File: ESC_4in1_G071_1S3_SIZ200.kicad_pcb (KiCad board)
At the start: 4 copper layers, 28 x 28 mm, 182 parts, among them J1 Conn_01x10, U1 STM32G071GBU6, U10 NCP81161MNTBG, U11 SIZ200DT-T1-GE3, U12 NCP81161MNTBG, U13 SIZ200DT-T1-GE3, U14 TPS630701, U15 TPS72733DSE, U16 INA186A2, U17 STM32G071GBU6, U18 NCP81161MNTBG, U19 SIZ200DT-T1-GE3, U2 NCP81161MNTBG, U20 NCP81161MNTBG, U21 STM32G071GBU6, U22 SIZ200DT-T1-GE3, U23 NCP81161MNTBG, U24 SIZ200DT-T1-GE3, U25 NCP81161MNTBG, U26 SIZ200DT-T1-GE3, U27 NCP81161MNTBG, U28 STM32G071GBU6, U29 SIZ200DT-T1-GE3, U3 SIZ200DT-T1-GE3, U30 NCP81161MNTBG, U31 SIZ200DT-T1-GE3, U4 NCP81161MNTBG, U5 SIZ200DT-T1-GE3, U6 NCP81161MNTBG, U7 SIZ200DT-T1-GE3, U8 NCP81161MNTBG, U9 SIZ200DT-T1-GE3

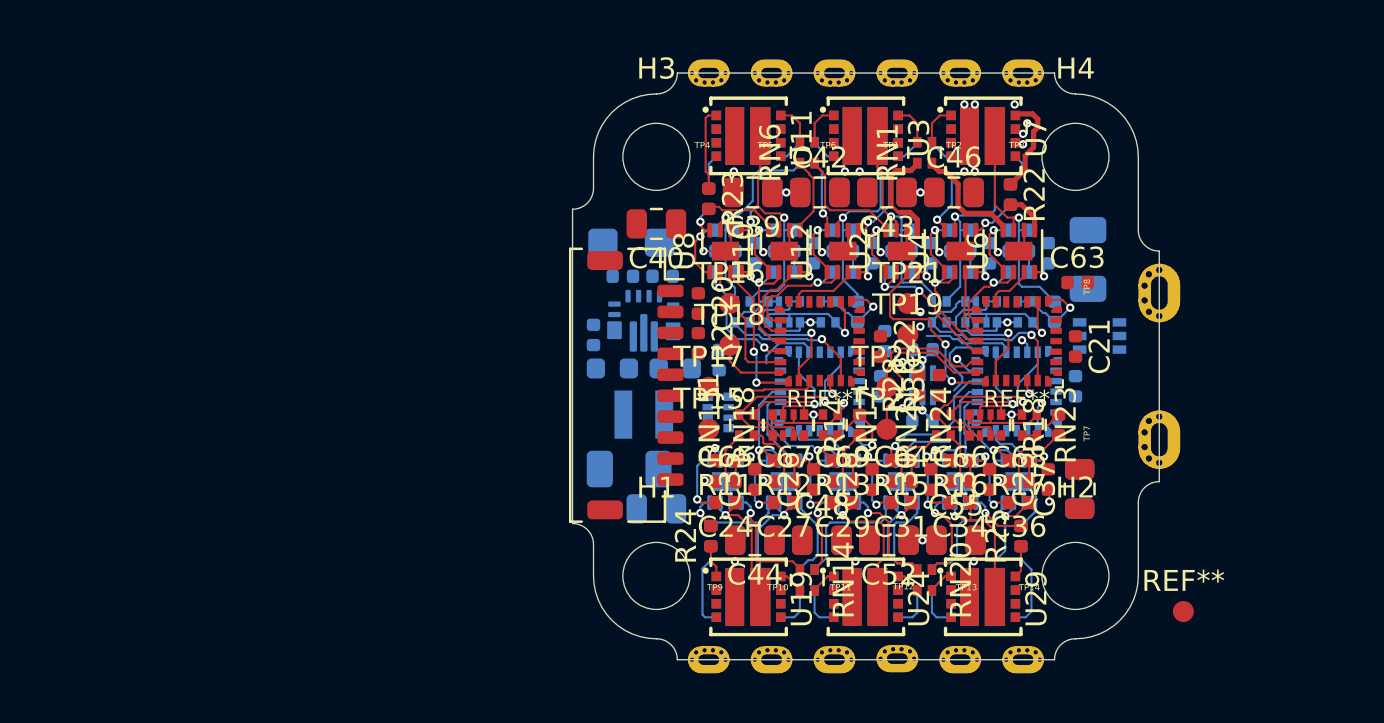
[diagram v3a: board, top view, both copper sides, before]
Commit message: update schematic and layout
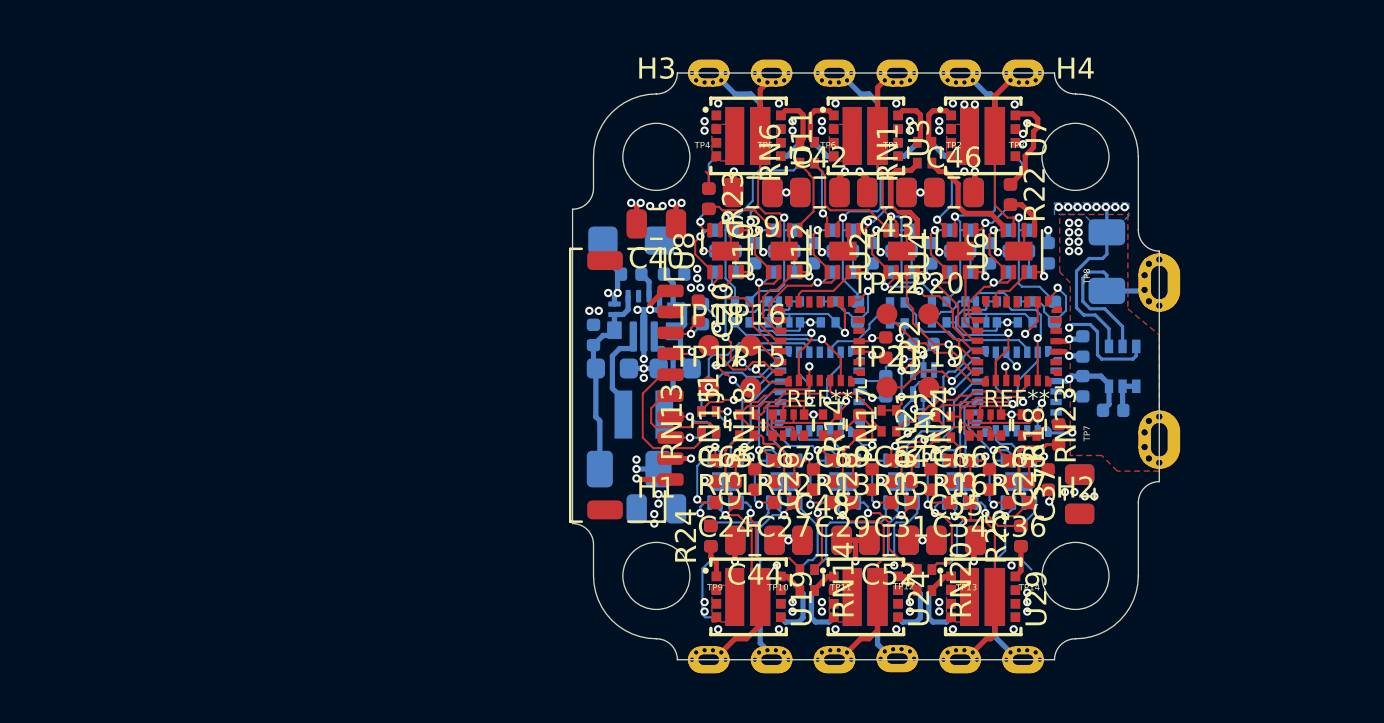
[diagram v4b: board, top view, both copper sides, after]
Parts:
- removed R27, R28, R29, R30: 1k, Resistor_SMD:R_0402_1005Metric
- removed REF**: TestPoint_Pad_D1.0mm_dense, 11_PSoC_FC_whoop:TestPoint_Pad_D1.0mm_dense
- added RN13: 1k, 11_PSoC_FC_whoop:R_Array_Convex_2x0402_dense, F.Cu at (128.5, 77.7)
- added RN16: 1k, 11_PSoC_FC_whoop:R_Array_Convex_2x0402_dense, B.Cu at (128.5, 77.7)
- added RN5: 1k, 11_PSoC_FC_whoop:R_Array_Convex_2x0402_dense, B.Cu at (137.5, 72.5)
- C21, C63, R2: moved to B.Cu
- RN2: footprint 11_PSoC_FC_whoop:R_Array_Convex_4x0402_dense -> 11_PSoC_FC_whoop:R_Array_Convex_2x0402_dense; moved to F.Cu
- moved RN2 8.16 mm to (137.1, 77.6), turned to 270 degrees
- moved C63 6.33 mm to (147.8, 77.1), turned to 180 degrees
- moved TP22 5.50 mm to (137.0, 72.5)
- moved TP21 4.12 mm to (137.0, 76.0)
- moved TP20 4.03 mm to (139.0, 72.5)
- moved TP15 2.83 mm to (130.5, 76.0)
- moved TP19 2.69 mm to (139.0, 76.0)
- moved TP16 2.24 mm to (130.5, 74.0)
- moved U16 1.82 mm to (148.2, 75.0), turned to 90 degrees
- moved R2 1.41 mm to (128.2, 72.5), turned to 90 degrees
- moved TP18 1.00 mm to (128.5, 74.0)
- moved R1 0.91 mm to (147.5, 70.0)
- moved FB2 0.56 mm to (126.8, 70.6), turned to 180 degrees
- moved TP8 0.50 mm to (150.0, 71.0)
- moved R18 0.45 mm to (145.2, 78.2)
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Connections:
- RN2 pad 1: /ESC1_IN -> /ESCx_tele
- RN2 pad 2: /ESC2_IN -> /ESCx_tele
- RN2 pad 3: /ESC3_IN -> /ESC2_tele_o
- RN2 pad 4: /ESC4_IN -> /ESC1_tele_o
- U1 pad 26: Net-(R30-Pad2) -> /ESC1_tele_o
- U17 pad 26: Net-(R28-Pad2) -> /ESC2_tele_o
- U21 pad 26: Net-(R27-Pad2) -> /ESC4_tele_o
- U28 pad 26: Net-(R29-Pad2) -> /ESC3_tele_o
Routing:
- net GND: track 53.2 -> 97.2 mm, vias 26 -> 76
- net Net-(R2-Pad2): track 0.00 -> 25.1 mm, vias 0 -> 2
- net +3V3: track 0.00 -> 21.4 mm, vias 1 -> 4
- net +BATT: track 0.00 -> 18.4 mm, vias 10 -> 44
- net /ESCx_tele: track 0.00 -> 18.0 mm, vias 0 -> 4
- net /ESC1_IN: track 0.00 -> 16.9 mm, vias 0 -> 2
- net /ESC3_IN: track 4.25 -> 17.5 mm, vias 0 -> 2
- net Net-(C13-Pad2): track 0.00 -> 9.12 mm
- net /ESC4_A_EN: track 0.00 -> 9.10 mm, vias 0 -> 2
- net Net-(R1-Pad2): track 0.00 -> 8.35 mm
- net /ESC2_IN: track 3.41 -> 11.1 mm, vias 0 -> 2
- net /ESC1_tele_o: track 0.00 -> 7.42 mm
- net Net-(J1-Pad5): track 0.00 -> 7.35 mm
- net /ESC3_tele_o: track 0.00 -> 7.23 mm
- net Net-(C15-Pad2): track 0.00 -> 5.83 mm
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- added copper zone on F.Cu, net +BATT
- added copper zone on B.Cu, net GND

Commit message: update layout
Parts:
- moved C63 0.15 mm to (147.8, 77.2)
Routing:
- net +BATT: track 18.4 -> 61.3 mm, vias 44 -> 45
- net GND: track 97.2 -> 128.0 mm, vias 76 -> 77
- net /ESC2_IN: track 11.1 -> 5.25 mm, vias 2 -> 0
- net /ESC2_B_GH: track 0.88 -> 5.05 mm
- net /ESC3_C_GL: track 1.32 -> 4.89 mm
- net Net-(C15-Pad2): track 5.83 -> 7.52 mm
- net /ESC4_SWDIO: track 1.76 -> 3.32 mm
- net /ESC4_SWDCLK: track 4.03 -> 5.49 mm
- net +5V: track 40.9 -> 41.7 mm
- net /ESC4_B_GH: track 4.15 -> 4.90 mm, vias 1 -> 0
- net /ESC4_IN: track 8.08 -> 8.78 mm
- net /ESC3_MC: track 3.41 -> 3.97 mm
- added copper zone on F.Cu, net GND

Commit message: update schematic, layout and schematic pdf
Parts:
- L1: value 1u -> 820 nH
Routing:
- added copper zone on In1.Cu_(power), net /ESC3_B
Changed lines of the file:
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@@
       (effects (font (size 1 1) (thickness 0.15)) (justify mirror))
     )
-    (fp_text value 1u (at 0 -2.65) (layer B.Fab)
+    (fp_text value "820 nH" (at 0 -2.65) (layer B.Fab)
       (effects (font (size 1 1) (thickness 0.15)) (justify mirror))
     )
@@
     (polygon
       (pts
-        (xy 150 89) (xy 122 89) (xy 122 61) (xy 150 61)
+        (xy 150 89.5) (xy 122 89.5) (xy 122 61) (xy 150 61)
       )
     )
@@
     (polygon
       (pts
-        (xy 150 89) (xy 122 89) (xy 122 80.5) (xy 144.5 80.5) (xy 145 80)
+        (xy 150 89.5) (xy 122 89.5) (xy 122 80.5) (xy 144.5 80.5) (xy 145 80)
         (xy 145 76.5) (xy 145.5 76) (xy 145.5 74) (xy 145 73.5) (xy 145 70)
         (xy 144.5 69.5) (xy 127 69.5) (xy 123 73.5) (xy 122 73.5) (xy 122 61)
@@
       )
     )
+  )
+  (zone (net 82) (net_name /ESC3_B) (layer "In1.Cu_(power)") (hatch edge 0.508)
+    (connect_pads yes (clearance 0.125))
+    (min_thickness 0.125)
+    (fill yes (arc_segments 32) (thermal_gap 0.508) (thermal_bridge_width 0.508))
+    (polygon
+      (pts
+        (xy 141.75 89.75) (xy 139.25 89.75) (xy 139.25 88.25) (xy 141.75 88.25)
+      )
+    )

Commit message: cosmetic update
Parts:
- added C70: 10u, Capacitor_SMD:C_0402_1005Metric, B.Cu at (133.1, 85.3)
- C13: footprint 11_PSoC_FC_whoop:C_1206_3216Metric_dense -> 11_PSoC_FC_whoop:C_0805_2012Metric_dense
- C37: moved to B.Cu
- moved TP14 22.5 mm to (122.0, 82.5), turned to 270 degrees
- moved TP3 22.5 mm to (150.0, 82.5), turned to 90 degrees
- moved TP4 22.5 mm to (150.0, 67.5), turned to 90 degrees
- moved TP9 22.5 mm to (122.0, 67.5), turned to 270 degrees
- moved TP10 20.8 mm to (122.0, 70.5), turned to 270 degrees
- moved TP2 20.8 mm to (150.0, 79.5), turned to 90 degrees
- moved TP13 20.8 mm to (122.0, 79.5), turned to 270 degrees
- moved TP5 20.8 mm to (150.0, 70.5), turned to 90 degrees
- moved TP8 20.6 mm to (140.0, 89.0), turned to 0 degrees
- moved TP7 20.4 mm to (132.5, 89.0), turned to 0 degrees
- moved H1 20.0 mm to (126.0, 65.0), turned to 270 degrees
- moved H2 20.0 mm to (126.0, 85.0), turned to 270 degrees
- moved H3 20.0 mm to (146.0, 65.0), turned to 270 degrees
- moved H4 20.0 mm to (146.0, 85.0), turned to 270 degrees
- moved TP1 19.9 mm to (150.0, 76.5), turned to 90 degrees
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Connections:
- net Net-(R1-Pad2) renamed /Batt-
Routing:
- net GND: track 128.0 -> 135.6 mm, vias 77 -> 80
- net +BATT: track 61.3 -> 67.6 mm, vias 45 -> 62
- net +3V3: track 21.5 -> 17.8 mm, vias 4 -> 5
- net /ESC2_A: track 14.1 -> 17.7 mm
- net /Batt-: track 8.44 -> 6.89 mm
- net +5V: track 41.7 -> 43.1 mm, vias 18 -> 17
- net /ESCx_tele: track 18.0 -> 19.0 mm
- net /ESC1_B_PWM: track 5.93 -> 4.98 mm
- net Net-(R2-Pad2): track 25.1 -> 25.8 mm
- net /ESC2_A_PWM: track 6.99 -> 6.45 mm
- net /ESC4_IN: track 8.78 -> 9.22 mm, vias 0 -> 2
- added copper zone on B.Cu, net +5V
- added copper zone on B.Cu, net +BATT
- added copper zone on B.Cu, net /Batt-
- added copper zone on F.Cu, net /ESC1_A
- added copper zone on F.Cu, net /ESC1_A_DRVH
- added copper zone on B.Cu, net /ESC1_B
- added copper zone on F.Cu, net /ESC1_C
- added copper zone on B.Cu, net /ESC2_A
- added copper zone on F.Cu, net /ESC2_B
- added copper zone on B.Cu, net /ESC2_C
- added copper zone on B.Cu, net /ESC3_A
- added copper zone on B.Cu, net /ESC3_A_DRVH
- added copper zone on B.Cu, net /ESC3_A_DRVL
- added copper zone on F.Cu, net /ESC3_B
- added copper zone on B.Cu, net /ESC3_C
- added copper zone on F.Cu, net /ESC4_A
- added copper zone on B.Cu, net /ESC4_B
- added copper zone on B.Cu, net /ESC4_B_DRVH
- added copper zone on B.Cu, net /ESC4_B_DRVL
- added copper zone on F.Cu, net /ESC4_C
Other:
- outline, holes or cut-outs redrawn
- rule solder_mask_min_width: 0.05 -> 0.1
- board text added: "+"
- board text added: "-"
- board text added: "ESC-4in1_G071_SIZ200"
- board text added: "Gnd VBat Ibat Tele ESC1 ESC2 ESC3 ESC4 5V Gnd"
- board text added: "crteensy 1-3S 15A"

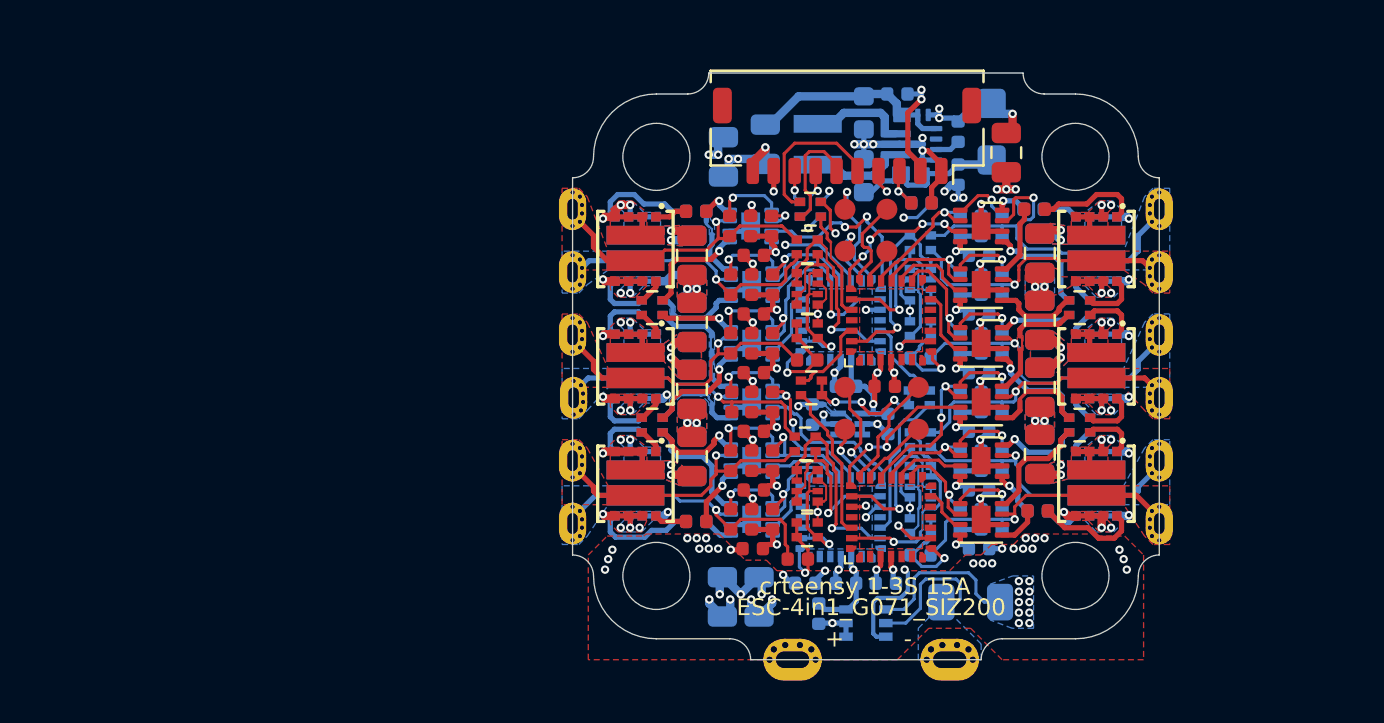
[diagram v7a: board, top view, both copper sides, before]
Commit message: update schematic, layout and doc
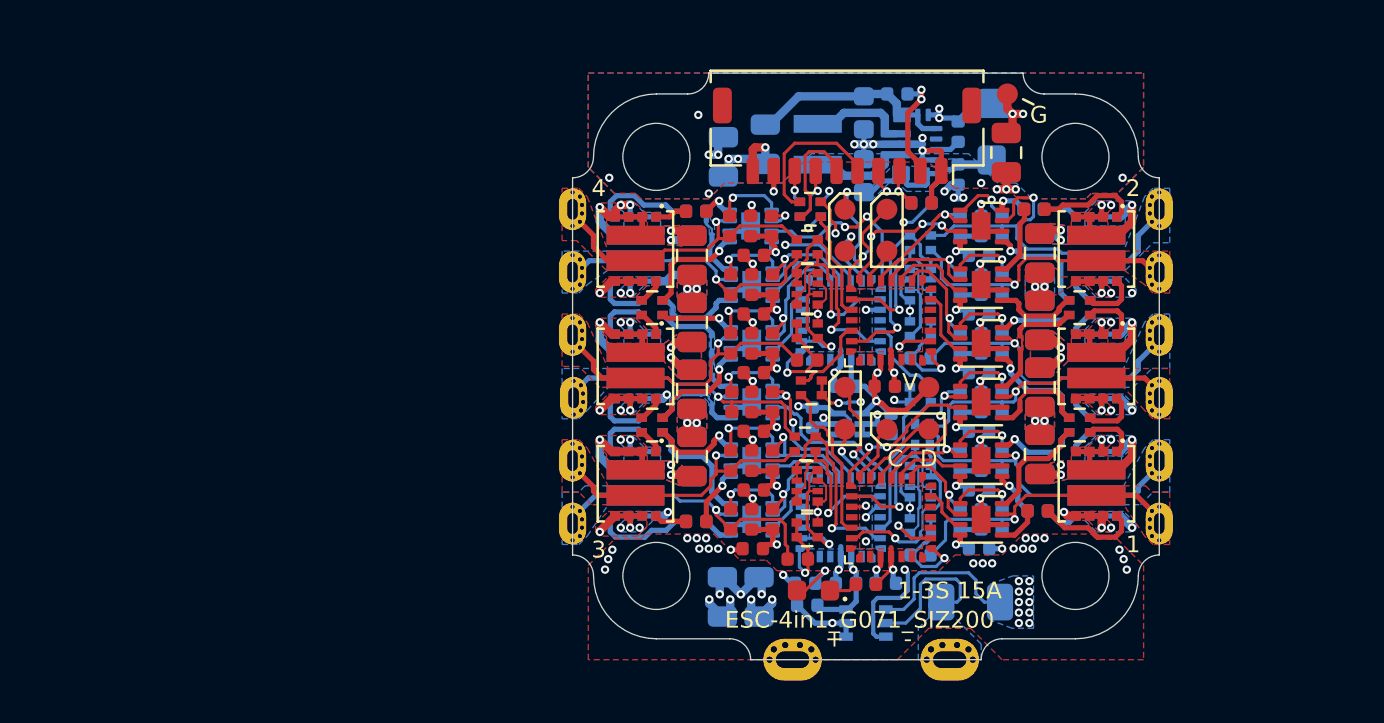
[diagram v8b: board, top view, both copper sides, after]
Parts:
- added D1: LED, LED_SMD:LED_0603_1608Metric, F.Cu at (133.5, 85.7)
- added R27: 1k, Resistor_SMD:R_0402_1005Metric, F.Cu at (136.0, 85.4)
- added TP23: TestPoint, 11_PSoC_FC_whoop:TestPoint_Pad_D1.0mm_dense, F.Cu at (139.0, 76.0)
- added TP24: TestPoint, 11_PSoC_FC_whoop:TestPoint_Pad_D1.0mm_dense, F.Cu at (142.8, 62.0)
- U11, U13, U19, U22, U24, U26, U29, U3, U31, U5, U7, U9: footprint 11_PSoC_FC_whoop:PowerPAIR3.3x3.3 -> 11_PSoC_FC_whoop:PowerPAIR3.3x3.3_splitpaste
- moved TP22 2.50 mm to (137.0, 78.0)
- moved C63 0.68 mm to (133.2, 86.4), turned to 0 degrees
- moved TP20 0.50 mm to (139.0, 78.0)
- moved RN8 0.27 mm to (138.7, 78.2), turned to 270 degrees
- moved RN5 0.16 mm to (138.6, 76.3)
- moved C18 0.15 mm to (133.4, 77.5)
- moved C19 0.15 mm to (137.2, 77.8)
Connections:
- RN8 pad 1: /ESC1_A -> /ESC1_B
- RN8 pad 2: /ESC1_B -> /ESC1_A
- RN8 pad 3: /ESC1_MB -> /ESC1_MA
- RN8 pad 4: /ESC1_MA -> /ESC1_MB
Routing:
- net +BATT: track 67.6 -> 86.1 mm
- net GND: track 135.6 -> 144.0 mm, vias 80 -> 87
- net +3V3: track 17.8 -> 22.0 mm
- net /ESC1_SWDCLK: track 5.41 -> 2.79 mm
- net /ESC1_B: track 14.0 -> 15.7 mm
- net Net-(D1-Pad1): track 0.00 -> 1.35 mm
- net /ESCx_tele: track 19.0 -> 17.8 mm
- net /ESC1_MA: track 9.95 -> 9.09 mm
- net /ESC1_SWDIO: track 3.39 -> 3.89 mm
- added copper zone on B.Cu, net Net-(C15-Pad2)
- removed copper zone on B.Cu, net +5V
- removed copper zone on In1.Cu_(power), net /ESC3_B
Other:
- board text added: "1-3S 15A"
- board text added: "C"
- board text added: "D"
- board text added: "G"
- board text added: "V"
- board text added: "crteensy"
- board text removed: "crteensy 1-3S 15A"
